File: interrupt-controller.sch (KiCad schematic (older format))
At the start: 5 parts

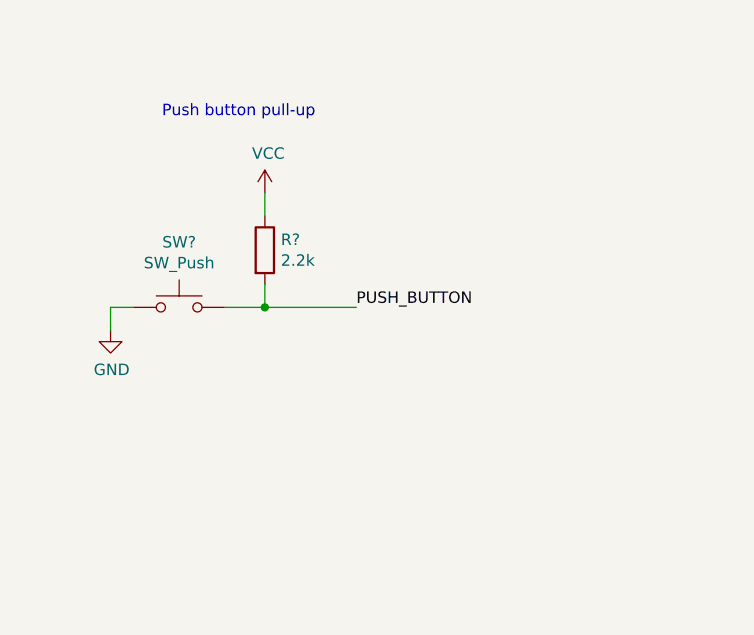
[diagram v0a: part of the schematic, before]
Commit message: Debounce pushbutton for 8259
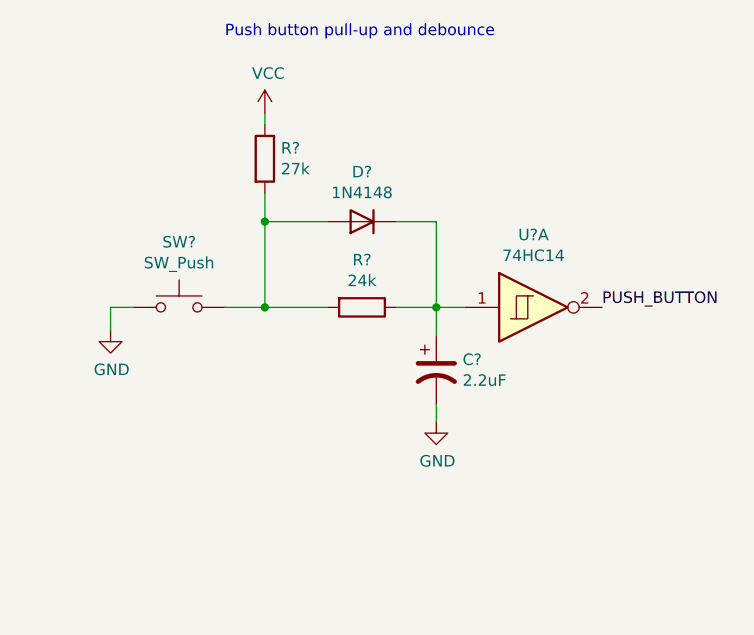
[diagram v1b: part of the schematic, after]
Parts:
- added C?: 2.2uF, symbol Device:CP1
- added D?: 1N4148, Diode_THT:D_DO-35_SOD27_P7.62mm_Horizontal, symbol Diode:1N4148
- added R?: 24k, symbol Device:R
- added U?: 74HC14, symbol 74xx:74HC14
- R?: value 2.2k -> 27k
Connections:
- net GND: now also C?.2
- net PUSH_BUTTON: now also U?.2; no longer R?.2, SW?.2
- new net: D?.2 (A), R?.2, R?.2, SW?.2
- new net: C?.1, D?.1 (K), R?.1, U?.1
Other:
- note added: "Push button pull-up and debounce"
- note removed: "Push button pull-up"
- moved on the sheet: R?
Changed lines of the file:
@@
 $Descr A4 11693 8268
 encoding utf-8
-Sheet 11 13
+Sheet 10 13
 Title "Interrupt Controller"
 Date ""
@@
 L Device:R R?
 U 1 1 61D074FC
-P 7500 2500
-F 0 "R?" H 7570 2546 50  0000 L CNN
-F 1 "2.2k" H 7570 2455 50  0000 L CNN
-F 2 "" V 7430 2500 50  0001 C CNN
-F 3 "~" H 7500 2500 50  0001 C CNN
-	1    7500 2500
-	1    0    0    -1
-$EndComp
-Wire Wire Line
-	7500 2650 7500 2750
+P 7500 2100
+F 0 "R?" H 7570 2146 50  0000 L CNN
+F 1 "27k" H 7570 2055 50  0000 L CNN
+F 2 "" V 7430 2100 50  0001 C CNN
+F 3 "~" H 7500 2100 50  0001 C CNN
+	1    7500 2100
+	1    0    0    -1
+$EndComp
+Wire Wire Line
+	7500 2250 7500 2375
 Wire Wire Line
 	7500 2750 7325 2750
 Wire Wire Line
-	7500 2350 7500 2250
+	7500 1950 7500 1900
 $Comp
 L power:VCC #PWR?
 U 1 1 61D08458
-P 7500 2250
-F 0 "#PWR?" H 7500 2100 50  0001 C CNN
-F 1 "VCC" H 7515 2423 50  0000 C CNN
-F 2 "" H 7500 2250 50  0001 C CNN
-F 3 "" H 7500 2250 50  0001 C CNN
-	1    7500 2250
-	1    0    0    -1
-$EndComp
-Wire Wire Line
-	7500 2750 7900 2750
+P 7500 1900
+F 0 "#PWR?" H 7500 1750 50  0001 C CNN
+F 1 "VCC" H 7515 2073 50  0000 C CNN
+F 2 "" H 7500 1900 50  0001 C CNN
+F 3 "" H 7500 1900 50  0001 C CNN
+	1    7500 1900
+	1    0    0    -1
+$EndComp
+Wire Wire Line
+	7500 2750 7775 2750
+Connection ~ 7500 2750
+Text Notes 7325 1575 0    50   ~ 0
+Push button pull-up and debounce
+$Comp
+L Device:R R?
+U 1 1 61D34260
+P 7925 2750
+F 0 "R?" V 7718 2750 50  0000 C CNN
+F 1 "24k" V 7809 2750 50  0000 C CNN
+F 2 "" V 7855 2750 50  0001 C CNN
+F 3 "~" H 7925 2750 50  0001 C CNN
+	1    7925 2750
+	0    1    1    0
+$EndComp
+$Comp
+L Diode:1N4148 D?
+U 1 1 61D371F9
+P 7925 2375
+F 0 "D?" H 7925 2158 50  0000 C CNN
+F 1 "1N4148" H 7925 2249 50  0000 C CNN
+F 2 "Diode_THT:D_DO-35_SOD27_P7.62mm_Horizontal" H 7925 2200 50  0001 C CNN
+F 3 "https://assets.nexperia.com/documents/data-sheet/1N4148_1N4448.pdf" H 7925 2375 50  0001 C CNN
+	1    7925 2375
+	-1   0    0    1
+$EndComp
+Wire Wire Line
+	7775 2375 7500 2375
+Connection ~ 7500 2375
+Wire Wire Line
+	7500 2375 7500 2750
+Wire Wire Line
+	8075 2750 8250 2750
+Wire Wire Line
+	8075 2375 8250 2375
+Wire Wire Line
+	8250 2375 8250 2750
+Connection ~ 8250 2750
+Wire Wire Line
+	8250 2750 8250 2875
+$Comp
+L Device:CP1 C?
+U 1 1 61D3CF7E
+P 8250 3025
+F 0 "C?" H 8365 3071 50  0000 L CNN
+F 1 "2.2uF" H 8365 2980 50  0000 L CNN
+F 2 "" H 8250 3025 50  0001 C CNN
+F 3 "~" H 8250 3025 50  0001 C CNN
+	1    8250 3025
+	1    0    0    -1
+$EndComp
+Wire Wire Line
+	8250 3175 8250 3250
+$Comp
+L power:GND #PWR?
+U 1 1 61D3DA48
+P 8250 3250
+F 0 "#PWR?" H 8250 3000 50  0001 C CNN
+F 1 "GND" H 8255 3077 50  0000 C CNN
+F 2 "" H 8250 3250 50  0001 C CNN
+F 3 "" H 8250 3250 50  0001 C CNN
+	1    8250 3250
+	1    0    0    -1
+$EndComp
+$Comp
+L 74xx:74HC14 U?
+U 1 1 61D413EB
+P 8675 2750
+F 0 "U?" H 8675 3067 50  0000 C CNN
+F 1 "74HC14" H 8675 2976 50  0000 C CNN
+F 2 "" H 8675 2750 50  0001 C CNN
+F 3 "http://www.ti.com/lit/gpn/sn74HC14" H 8675 2750 50  0001 C CNN
+	1    8675 2750
+	1    0    0    -1
+$EndComp
+Wire Wire Line
+	8375 2750 8250 2750
 Wire Bus Line
 	2975 2750 2975 3550
-Connection ~ 7500 2750
-Text Label 7900 2750 0    50   ~ 0
+Text Label 8975 2750 0    50   ~ 0
 PUSH_BUTTON
-Text Notes 7050 1925 0    50   ~ 0
-Push button pull-up
 $EndSCHEMATC

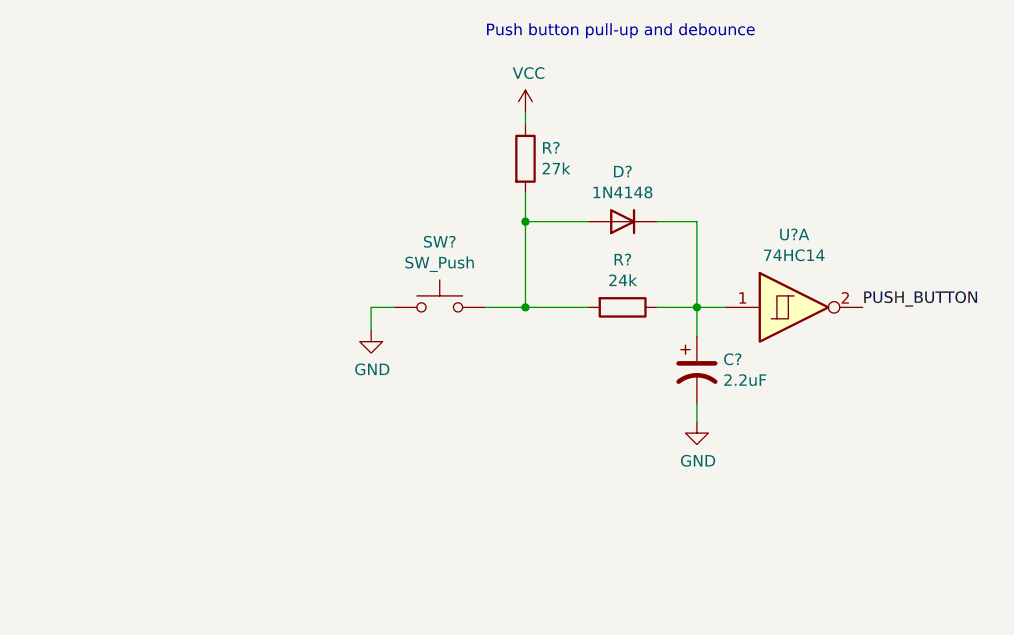
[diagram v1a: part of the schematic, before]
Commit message: IO address decoding
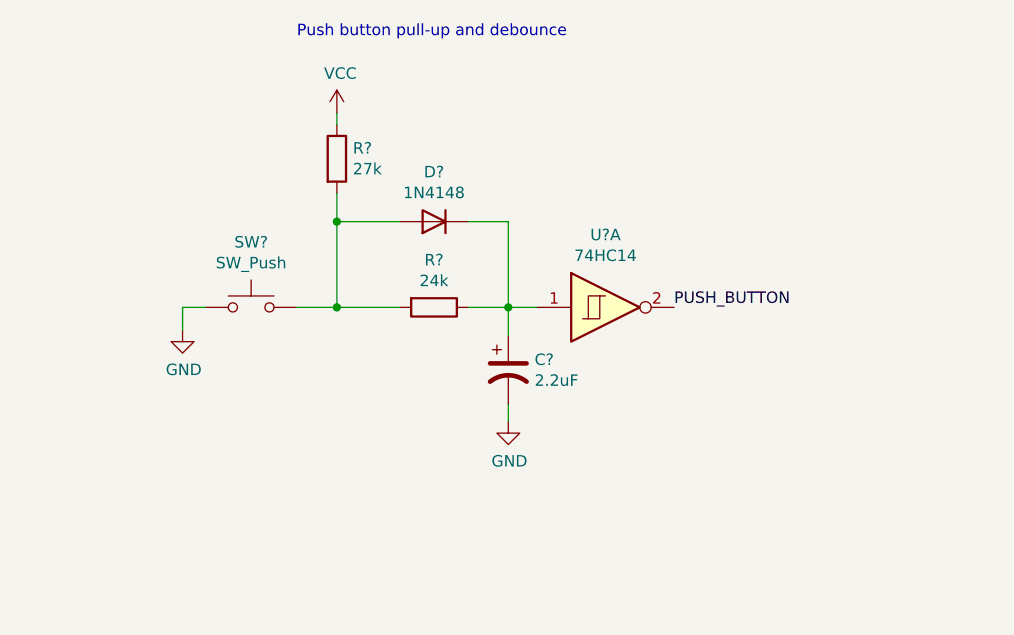
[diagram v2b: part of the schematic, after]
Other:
- moved on the sheet: C?, D?, R?, SW?, U?A
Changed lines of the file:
@@
 $Descr A4 11693 8268
 encoding utf-8
-Sheet 10 13
+Sheet 10 14
 Title "Interrupt Controller"
 Date ""
@@
 L Switch:SW_Push SW?
 U 1 1 61D05D5A
-P 7125 2750
-F 0 "SW?" H 7125 3035 50  0000 C CNN
-F 1 "SW_Push" H 7125 2944 50  0000 C CNN
-F 2 "" H 7125 2950 50  0001 C CNN
-F 3 "~" H 7125 2950 50  0001 C CNN
-	1    7125 2750
+P 6300 2750
+F 0 "SW?" H 6300 3035 50  0000 C CNN
+F 1 "SW_Push" H 6300 2944 50  0000 C CNN
+F 2 "" H 6300 2950 50  0001 C CNN
+F 3 "~" H 6300 2950 50  0001 C CNN
+	1    6300 2750
 	1    0    0    -1
 $EndComp
@@
 L power:GND #PWR?
 U 1 1 61D06DE7
-P 6825 2850
-F 0 "#PWR?" H 6825 2600 50  0001 C CNN
-F 1 "GND" H 6830 2677 50  0000 C CNN
-F 2 "" H 6825 2850 50  0001 C CNN
-F 3 "" H 6825 2850 50  0001 C CNN
-	1    6825 2850
-	1    0    0    -1
-$EndComp
-Wire Wire Line
-	6825 2850 6825 2750
-Wire Wire Line
-	6825 2750 6925 2750
+P 6000 2850
+F 0 "#PWR?" H 6000 2600 50  0001 C CNN
+F 1 "GND" H 6005 2677 50  0000 C CNN
+F 2 "" H 6000 2850 50  0001 C CNN
+F 3 "" H 6000 2850 50  0001 C CNN
+	1    6000 2850
+	1    0    0    -1
+$EndComp
+Wire Wire Line
+	6000 2850 6000 2750
+Wire Wire Line
+	6000 2750 6100 2750
 $Comp
 L Device:R R?
 U 1 1 61D074FC
-P 7500 2100
-F 0 "R?" H 7570 2146 50  0000 L CNN
-F 1 "27k" H 7570 2055 50  0000 L CNN
-F 2 "" V 7430 2100 50  0001 C CNN
-F 3 "~" H 7500 2100 50  0001 C CNN
-	1    7500 2100
-	1    0    0    -1
-$EndComp
-Wire Wire Line
-	7500 2250 7500 2375
-Wire Wire Line
-	7500 2750 7325 2750
-Wire Wire Line
-	7500 1950 7500 1900
+P 6675 2100
+F 0 "R?" H 6745 2146 50  0000 L CNN
+F 1 "27k" H 6745 2055 50  0000 L CNN
+F 2 "" V 6605 2100 50  0001 C CNN
+F 3 "~" H 6675 2100 50  0001 C CNN
+	1    6675 2100
+	1    0    0    -1
+$EndComp
+Wire Wire Line
+	6675 2250 6675 2375
+Wire Wire Line
+	6675 2750 6500 2750
+Wire Wire Line
+	6675 1950 6675 1900
 $Comp
 L power:VCC #PWR?
 U 1 1 61D08458
-P 7500 1900
-F 0 "#PWR?" H 7500 1750 50  0001 C CNN
-F 1 "VCC" H 7515 2073 50  0000 C CNN
-F 2 "" H 7500 1900 50  0001 C CNN
-F 3 "" H 7500 1900 50  0001 C CNN
-	1    7500 1900
-	1    0    0    -1
-$EndComp
-Wire Wire Line
-	7500 2750 7775 2750
-Connection ~ 7500 2750
-Text Notes 7325 1575 0    50   ~ 0
+P 6675 1900
+F 0 "#PWR?" H 6675 1750 50  0001 C CNN
+F 1 "VCC" H 6690 2073 50  0000 C CNN
+F 2 "" H 6675 1900 50  0001 C CNN
+F 3 "" H 6675 1900 50  0001 C CNN
+	1    6675 1900
+	1    0    0    -1
+$EndComp
+Wire Wire Line
+	6675 2750 6950 2750
+Connection ~ 6675 2750
+Text Notes 6500 1575 0    50   ~ 0
 Push button pull-up and debounce
 $Comp
 L Device:R R?
 U 1 1 61D34260
-P 7925 2750
-F 0 "R?" V 7718 2750 50  0000 C CNN
-F 1 "24k" V 7809 2750 50  0000 C CNN
-F 2 "" V 7855 2750 50  0001 C CNN
-F 3 "~" H 7925 2750 50  0001 C CNN
-	1    7925 2750
+P 7100 2750
+F 0 "R?" V 6893 2750 50  0000 C CNN
+F 1 "24k" V 6984 2750 50  0000 C CNN
+F 2 "" V 7030 2750 50  0001 C CNN
+F 3 "~" H 7100 2750 50  0001 C CNN
+	1    7100 2750
 	0    1    1    0
 $EndComp
@@
 L Diode:1N4148 D?
 U 1 1 61D371F9
-P 7925 2375
-F 0 "D?" H 7925 2158 50  0000 C CNN
-F 1 "1N4148" H 7925 2249 50  0000 C CNN
-F 2 "Diode_THT:D_DO-35_SOD27_P7.62mm_Horizontal" H 7925 2200 50  0001 C CNN
-F 3 "https://assets.nexperia.com/documents/data-sheet/1N4148_1N4448.pdf" H 7925 2375 50  0001 C CNN
-	1    7925 2375
+P 7100 2375
+F 0 "D?" H 7100 2158 50  0000 C CNN
+F 1 "1N4148" H 7100 2249 50  0000 C CNN
+F 2 "Diode_THT:D_DO-35_SOD27_P7.62mm_Horizontal" H 7100 2200 50  0001 C CNN
+F 3 "https://assets.nexperia.com/documents/data-sheet/1N4148_1N4448.pdf" H 7100 2375 50  0001 C CNN
+	1    7100 2375
 	-1   0    0    1
 $EndComp
 Wire Wire Line
-	7775 2375 7500 2375
-Connection ~ 7500 2375
-Wire Wire Line
-	7500 2375 7500 2750
-Wire Wire Line
-	8075 2750 8250 2750
-Wire Wire Line
-	8075 2375 8250 2375
-Wire Wire Line
-	8250 2375 8250 2750
-Connection ~ 8250 2750
-Wire Wire Line
-	8250 2750 8250 2875
+	6950 2375 6675 2375
+Connection ~ 6675 2375
+Wire Wire Line
+	6675 2375 6675 2750
+Wire Wire Line
+	7250 2750 7425 2750
+Wire Wire Line
+	7250 2375 7425 2375
+Wire Wire Line
+	7425 2375 7425 2750
+Connection ~ 7425 2750
+Wire Wire Line
+	7425 2750 7425 2875
 $Comp
 L Device:CP1 C?
 U 1 1 61D3CF7E
-P 8250 3025
-F 0 "C?" H 8365 3071 50  0000 L CNN
-F 1 "2.2uF" H 8365 2980 50  0000 L CNN
-F 2 "" H 8250 3025 50  0001 C CNN
-F 3 "~" H 8250 3025 50  0001 C CNN
-	1    8250 3025
-	1    0    0    -1
-$EndComp
-Wire Wire Line
-	8250 3175 8250 3250
+P 7425 3025
+F 0 "C?" H 7540 3071 50  0000 L CNN
+F 1 "2.2uF" H 7540 2980 50  0000 L CNN
+F 2 "" H 7425 3025 50  0001 C CNN
+F 3 "~" H 7425 3025 50  0001 C CNN
+	1    7425 3025
+	1    0    0    -1
+$EndComp
+Wire Wire Line
+	7425 3175 7425 3250
 $Comp
 L power:GND #PWR?
 U 1 1 61D3DA48
-P 8250 3250
-F 0 "#PWR?" H 8250 3000 50  0001 C CNN
-F 1 "GND" H 8255 3077 50  0000 C CNN
-F 2 "" H 8250 3250 50  0001 C CNN
-F 3 "" H 8250 3250 50  0001 C CNN
-	1    8250 3250
+P 7425 3250
+F 0 "#PWR?" H 7425 3000 50  0001 C CNN
+F 1 "GND" H 7430 3077 50  0000 C CNN
+F 2 "" H 7425 3250 50  0001 C CNN
+F 3 "" H 7425 3250 50  0001 C CNN
+	1    7425 3250
 	1    0    0    -1
 $EndComp
@@
 L 74xx:74HC14 U?
 U 1 1 61D413EB
-P 8675 2750
-F 0 "U?" H 8675 3067 50  0000 C CNN
-F 1 "74HC14" H 8675 2976 50  0000 C CNN
-F 2 "" H 8675 2750 50  0001 C CNN
-F 3 "http://www.ti.com/lit/gpn/sn74HC14" H 8675 2750 50  0001 C CNN
-	1    8675 2750
-	1    0    0    -1
-$EndComp
-Wire Wire Line
-	8375 2750 8250 2750
+P 7850 2750
+F 0 "U?" H 7850 3067 50  0000 C CNN
+F 1 "74HC14" H 7850 2976 50  0000 C CNN
+F 2 "" H 7850 2750 50  0001 C CNN
+F 3 "http://www.ti.com/lit/gpn/sn74HC14" H 7850 2750 50  0001 C CNN
+	1    7850 2750
+	1    0    0    -1
+$EndComp
+Wire Wire Line
+	7550 2750 7425 2750
+Text Label 8150 2750 0    50   ~ 0
+PUSH_BUTTON
 Wire Bus Line
 	2975 2750 2975 3550
-Text Label 8975 2750 0    50   ~ 0
-PUSH_BUTTON
 $EndSCHEMATC

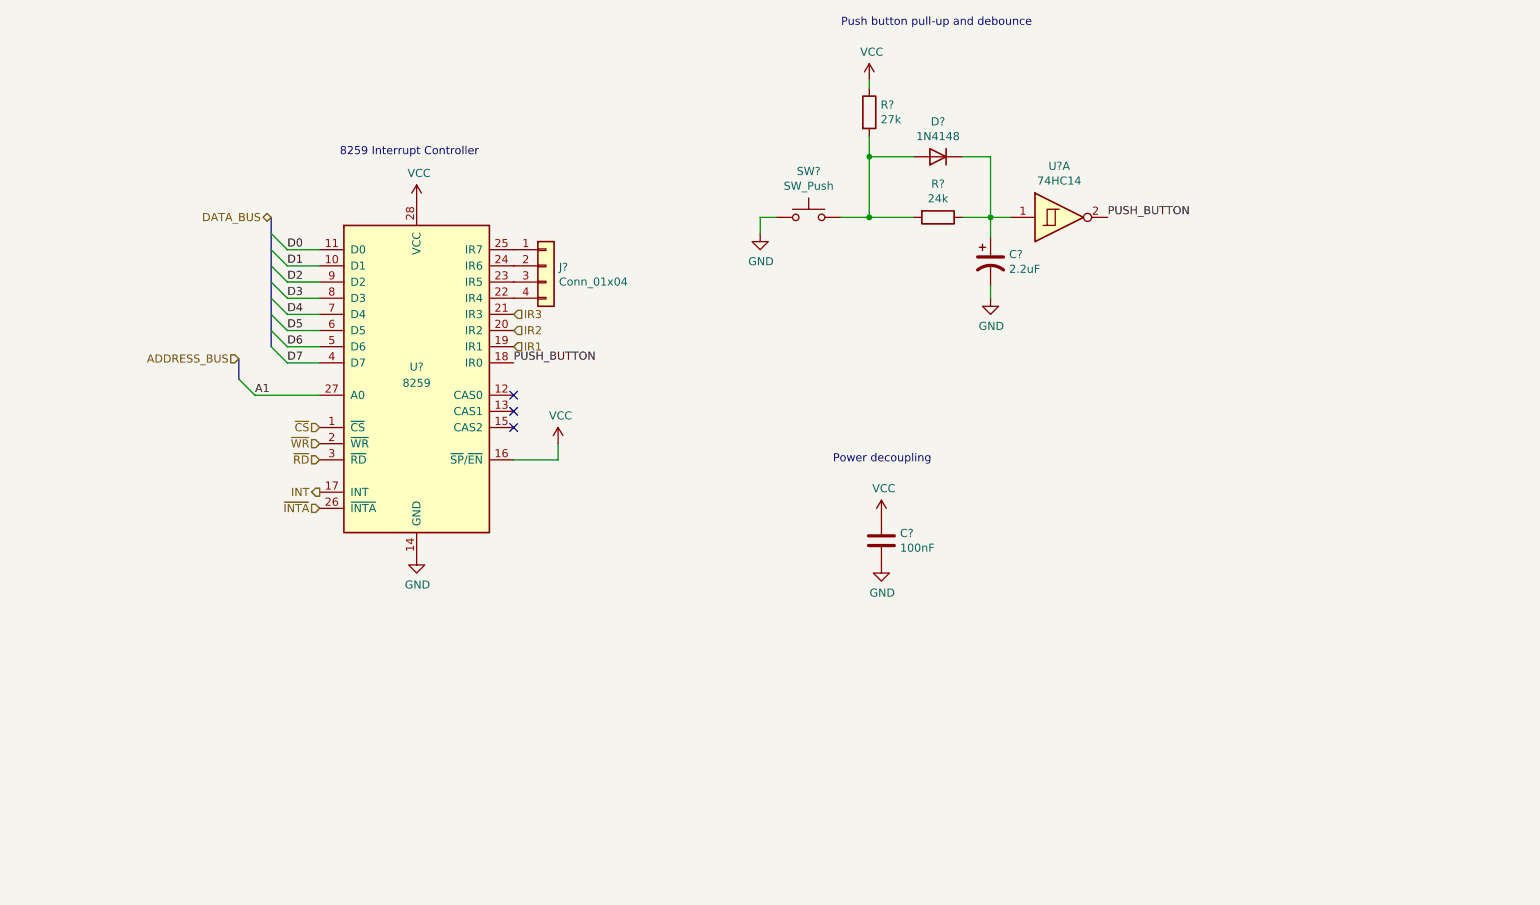
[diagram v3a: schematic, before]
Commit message: General edits; removed floating inputs
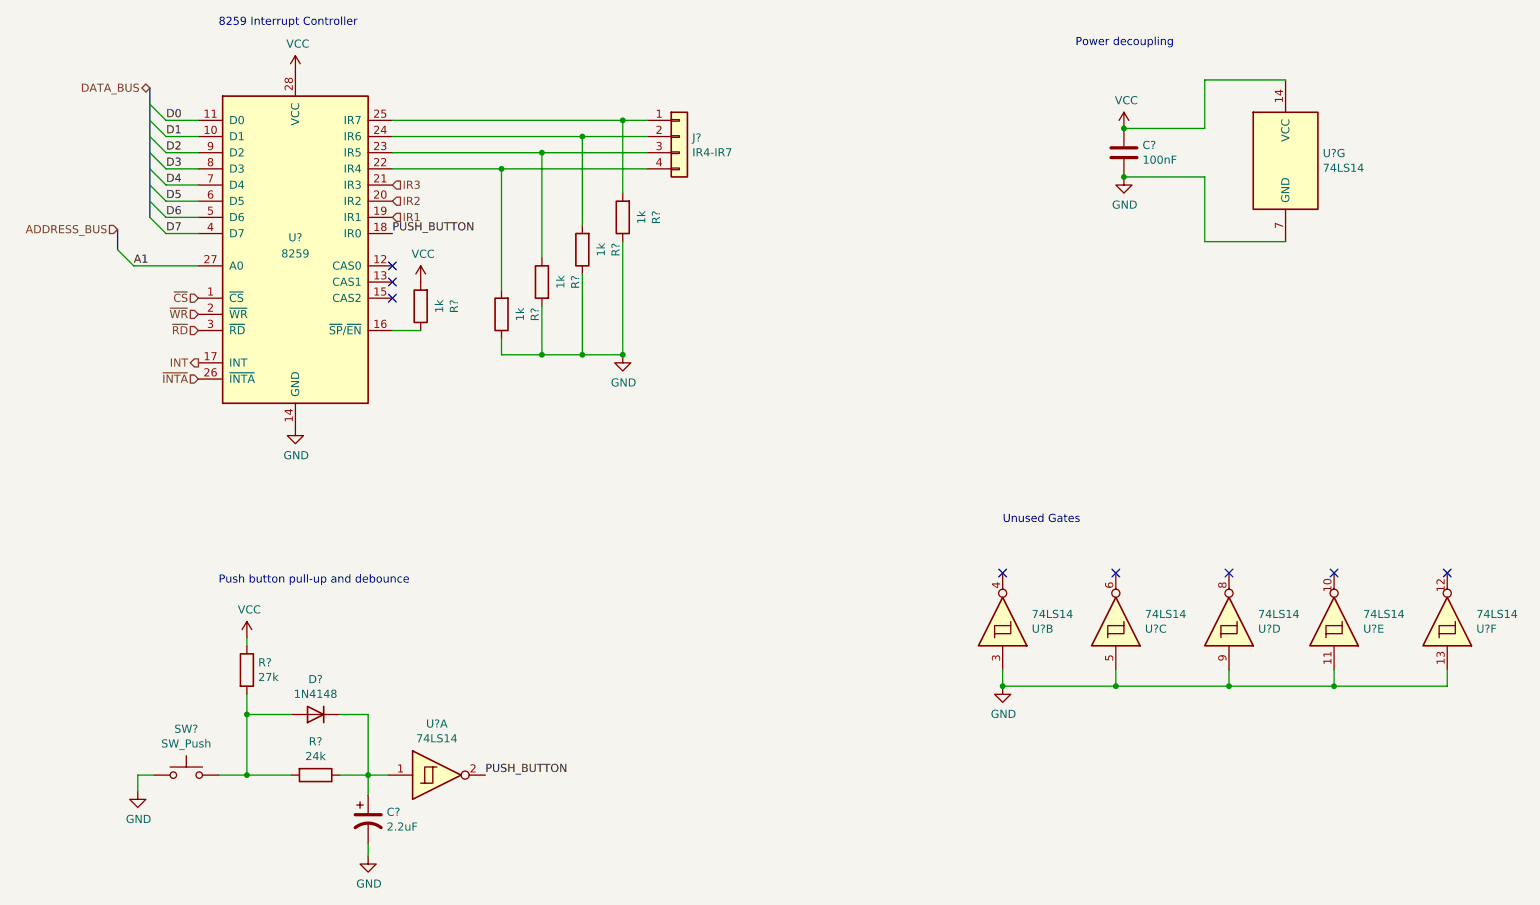
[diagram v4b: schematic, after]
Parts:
- removed C?: 2.2uF, symbol Device:CP1
- removed D?: 1N4148, Diode_THT:D_DO-35_SOD27_P7.62mm_Horizontal, symbol Diode:1N4148
- removed R?: 27k, symbol Device:R
- removed R?: 24k, symbol Device:R
- removed SW?: SW_Push, symbol Switch:SW_Push
- removed U?: 74HC14, symbol 74xx:74HC14
- added C?: 2.2uF, symbol Device:CP1
- added D?: 1N4148, Diode_THT:D_DO-35_SOD27_P7.62mm_Horizontal, symbol Diode:1N4148
- added R? (x5): 1k, symbol Device:R
- added R?: 27k, symbol Device:R
- added R?: 24k, symbol Device:R
- added SW?: SW_Push, symbol Switch:SW_Push
- added U? (x7): 74LS14, symbol 74xx:74LS14
- J?: value Conn_01x04 -> IR4-IR7
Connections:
- net GND: now also C?.2, R?.1, R?.1, R?.1, R?.2, SW?.1, U?.11, U?.13, U?.3, U?.5, U?.7 (GND), U?.9
- net PUSH_BUTTON: now also U?.2
- net VCC: now also R?.1, R?.2, U?.14 (VCC); no longer U?.16 (~SP~/~EN~)
- net at J?.4 (Pin_4), U?.22 (IR4): now also R?.2
- net at J?.3 (Pin_3), U?.23 (IR5): now also R?.1
- net at J?.2 (Pin_2), U?.24 (IR6): now also R?.2
- net at J?.1 (Pin_1), U?.25 (IR7): now also R?.2
- new net: R?.1, U?.16 (~SP~/~EN~)
- new net: D?.2 (A), R?.2, R?.2, SW?.2
- new net: C?.1, D?.1 (K), R?.1, U?.1
- no-connect marks 3 -> 8
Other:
- note added: "Unused Gates"
- moved on the sheet: C?, J?, U?

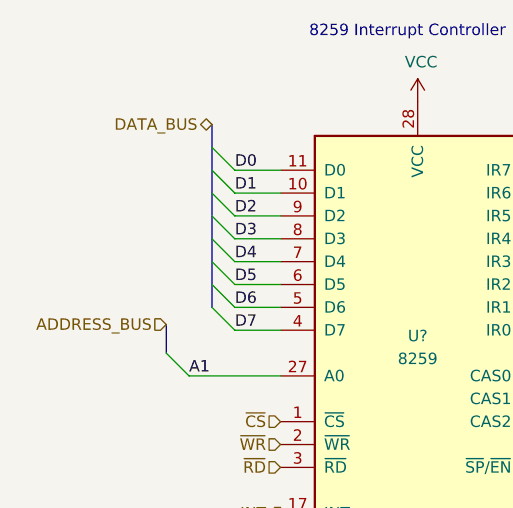
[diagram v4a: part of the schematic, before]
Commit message: Updates to pass ERC
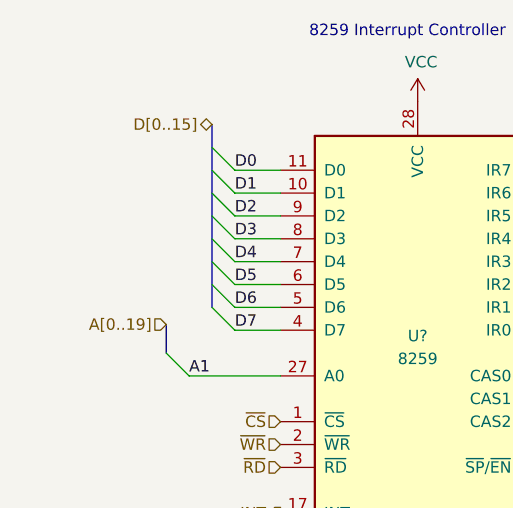
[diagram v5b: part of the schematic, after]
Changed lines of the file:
@@
 8259 Interrupt Controller
 Text HLabel 2025 2825 0    50   Input ~ 0
-ADDRESS_BUS
+A[0..19]
 Wire Bus Line
 	2025 2950 2025 2825
@@
 ~CS
 Text HLabel 2225 1950 0    50   BiDi ~ 0
-DATA_BUS
+D[0..15]
 Entry Wire Line
 	2225 2750 2325 2850
